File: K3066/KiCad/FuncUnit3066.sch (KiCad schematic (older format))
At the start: 18 parts, among them J11 PAD, J12 PAD, J14 PAD, J16 PAD, J18 PAD, J19 PAD, Q11 SSM3K7002BFU, Q12 SSM6N7002BFE, Q13 SSM6N7002BFE, Q14 SSM6N7002BFE

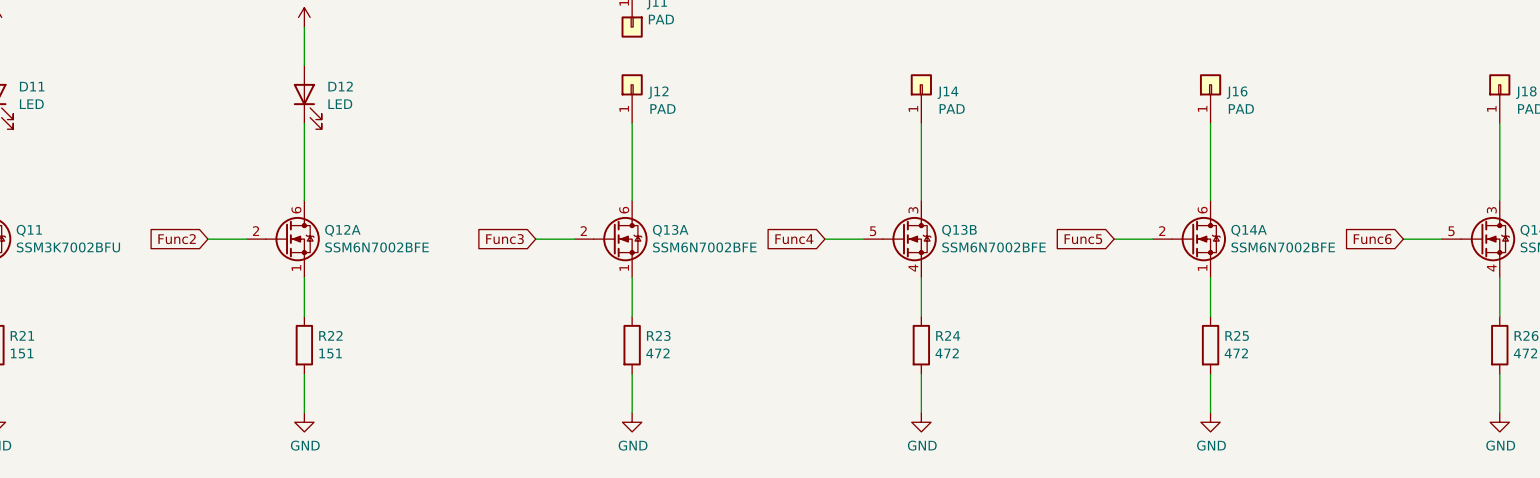
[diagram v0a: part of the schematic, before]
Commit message: 回路の問題点を修正 (K3066: Rev3 / それ以外: Rev2)
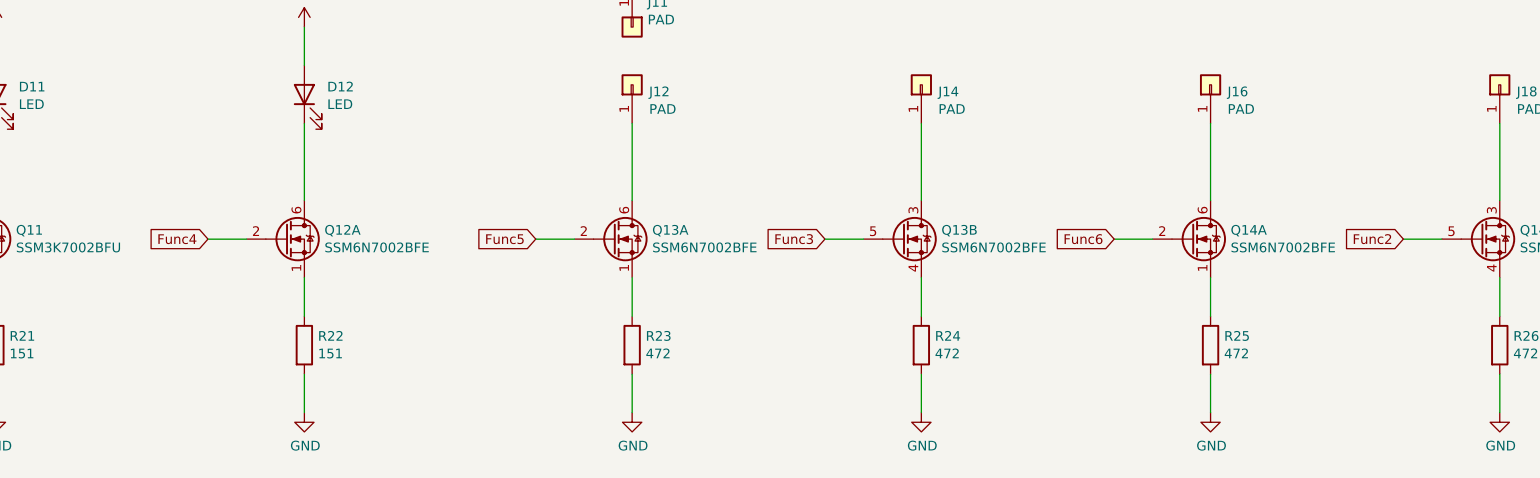
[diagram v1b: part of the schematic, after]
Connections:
- net Func2: now also Q14.5 (G); no longer Q12.2 (G)
- net Func3: now also Q13.5 (G); no longer Q13.2 (G)
- net Func4: now also Q12.2 (G); no longer Q13.5 (G)
- net Func5: now also Q13.2 (G); no longer Q14.2 (G)
- net Func6: now also Q14.2 (G); no longer Q14.5 (G)
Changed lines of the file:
@@
 Func1
 Text GLabel 4800 2600 0    50   Input ~ 0
-Func3
+Func5
 Wire Wire Line
 	5000 2600 4800 2600
@@
 	6800 3000 6800 2800
 Text GLabel 6300 2600 0    50   Input ~ 0
-Func4
+Func3
 Wire Wire Line
 	6500 2600 6300 2600
@@
 	8300 3000 8300 2800
 Text GLabel 7800 2600 0    50   Input ~ 0
-Func5
+Func6
 Wire Wire Line
 	8000 2600 7800 2600
@@
 	9800 3000 9800 2800
 Text GLabel 9300 2600 0    50   Input ~ 0
-Func6
+Func2
 Wire Wire Line
 	9500 2600 9300 2600
@@
 	3600 3300 3600 3500
 Text GLabel 3100 2600 0    50   Input ~ 0
-Func2
+Func4
 Wire Wire Line
 	3300 2600 3100 2600
